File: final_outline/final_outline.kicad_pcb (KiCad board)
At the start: 2 copper layers, 99.5 x 90 mm, 32 parts, among them P001 CANCONNECTOR, P002 AUXCONNECTOR, P100 ISP, P101 DEBUG_LED, U401 ISO1050, U403 LPC11C14, U404 MCP2515_TSSOP, U405 ISO1050, U501 MCP1755

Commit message: board routing in progress
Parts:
- removed C407, C408: 0.1uF, Capacitors_SMD:C_0603_HandSoldering
- removed C409, C410, C411, C412: 1uF, Capacitors_SMD:C_0805_HandSoldering
- removed U404: MCP2515_TSSOP, Housings_SSOP:TSSOP-20_4.4x6.5mm_Pitch0.65mm
- removed U405: ISO1050, Housings_SSOP:MSOP-8_3x3mm_Pitch0.65mm
- moved R201 41.8 mm to (122.6, 108.6)
- moved R401 25.8 mm to (110.5, 47.6), turned to 0 degrees
- moved R402 24.1 mm to (110.5, 50.8), turned to 0 degrees
- moved C406 15.3 mm to (132.1, 78.7), turned to 270 degrees
- moved U501 12.8 mm to (142.2, 101.9)
- moved C404 9.02 mm to (118.1, 94.0)
- moved C405 8.95 mm to (129.5, 78.7), turned to 270 degrees
- moved C401 8.49 mm to (123.8, 94.0)
- moved C402 7.96 mm to (123.2, 96.5)
- moved R303 7.87 mm to (171.4, 57.1), turned to 270 degrees
- moved R305 7.87 mm to (179.1, 57.1), turned to 270 degrees
- moved R306 7.87 mm to (182.9, 57.1)
- moved R302 7.70 mm to (167.6, 57.1), turned to 270 degrees
- moved R307 7.70 mm to (186.7, 57.1), turned to 270 degrees
- moved U401 7.62 mm to (120.7, 101.8)
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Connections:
- net Net-(U401-Pad2) renamed /Micro_Controller/CAN_RXD
- net Net-(U401-Pad3) renamed /Micro_Controller/CAN_TXD
- C401 pad 1: /BACK_PANEL/CANH -> +5V
- C402 pad 1: /BACK_PANEL/CANH -> +5V
- C403 pad 1: /Micro_Controller/+3V3 -> +3V3
- C404 pad 1: /Micro_Controller/+3V3 -> +3V3
- C405 pad 1: /Micro_Controller/+3V3 -> +3V3
- C406 pad 1: /Micro_Controller/+3V3 -> +3V3
- P001 pad 1: Net-(P001-Pad1) -> /BACK_PANEL/CANL
- P001 pad 2: Net-(P001-Pad1) -> /BACK_PANEL/CANH
- P001 pad 3: /BACK_PANEL/CANH -> GND
- P001 pad 4: /BACK_PANEL/CANH -> +5V
- P001 pad 5: GND -> +5V
- P001 pad 7: Net-(P001-Pad7) -> /BACK_PANEL/CANL
- P001 pad 8: Net-(P001-Pad7) -> /BACK_PANEL/CANH
- P100 pad 1: /FRONT_PANEL/+5V -> /FRONT_PANEL/MCU_RESET_N
- P100 pad 2: /FRONT_PANEL/RXD -> GND
- P100 pad 3: /FRONT_PANEL/TXD -> /FRONT_PANEL/RXD
- P100 pad 4: /FRONT_PANEL/MCU_RESET_N -> /FRONT_PANEL/MCU_PROG_N
- P100 pad 5: /FRONT_PANEL/MCU_PROG_N -> +5V
- P100 pad 6: GND -> /FRONT_PANEL/TXD
- P101 pad 11: GND -> Net-(P101-Pad11)
- P101 pad 13: GND -> Net-(P101-Pad13)
- P101 pad 15: GND -> Net-(P101-Pad15)
- P101 pad 2: Net-(P101-Pad2) -> GND
- P101 pad 4: Net-(P101-Pad4) -> GND
- P101 pad 6: Net-(P101-Pad6) -> GND
- P101 pad 8: Net-(P101-Pad8) -> GND
- P101 pad 9: GND -> Net-(P101-Pad9)
- R201 pad 1: /BACK_PANEL/CANH -> /BACK_PANEL/CANL
- R201 pad 2: GND -> /BACK_PANEL/CANH
- R301 pad 2: Net-(P101-Pad2) -> Net-(P101-Pad9)
- R302 pad 1: /FRONT_PANEL/LED2 -> Net-(P101-Pad10)
- R302 pad 2: Net-(P101-Pad6) -> /FRONT_PANEL/LED1
- R303 pad 1: /FRONT_PANEL/LED4 -> Net-(P101-Pad11)
- R303 pad 2: Net-(P101-Pad10) -> /FRONT_PANEL/LED2
- R304 pad 1: /FRONT_PANEL/LED6 -> /FRONT_PANEL/LED3
- R304 pad 2: Net-(P101-Pad14) -> Net-(P101-Pad12)
- R305 pad 1: /FRONT_PANEL/LED1 -> Net-(P101-Pad13)
- R305 pad 2: Net-(P101-Pad4) -> /FRONT_PANEL/LED4
- R306 pad 1: /FRONT_PANEL/LED3 -> /FRONT_PANEL/LED5
- R306 pad 2: Net-(P101-Pad8) -> Net-(P101-Pad14)
- R307 pad 1: /FRONT_PANEL/LED5 -> Net-(P101-Pad15)
- R307 pad 2: Net-(P101-Pad12) -> /FRONT_PANEL/LED6
- R401 pad 1: /Micro_Controller/+3V3 -> +3V3
- R402 pad 1: /Micro_Controller/+3V3 -> +3V3
- U401 pad 1: /Micro_Controller/+3V3 -> +3V3
- U401 pad 6: GND -> /BACK_PANEL/CANL
- U401 pad 8: /BACK_PANEL/CANH -> +5V
- U403 pad 1: /FRONT_PANEL/LED1 -> /FRONT_PANEL/LED3
- U403 pad 11: /FRONT_PANEL/LED2 -> /FRONT_PANEL/LED1
- U403 pad 12: /FRONT_PANEL/LED3 -> /FRONT_PANEL/LED0
- U403 pad 36: /FRONT_PANEL/LED4 -> /FRONT_PANEL/LED7
- U403 pad 37: /FRONT_PANEL/LED5 -> /FRONT_PANEL/LED6
- U403 pad 43: /FRONT_PANEL/LED6 -> /FRONT_PANEL/LED5
- U403 pad 44: /Micro_Controller/+3V3 -> +3V3
- U403 pad 48: /FRONT_PANEL/LED7 -> /FRONT_PANEL/LED4
- U403 pad 8: /Micro_Controller/+3V3 -> +3V3
- U403 pad 9: /FRONT_PANEL/LED0 -> /FRONT_PANEL/LED2
- U501 pad 1: /FRONT_PANEL/+5V -> +5V
- U501 pad 3: /FRONT_PANEL/+5V -> +5V
- U501 pad 5: /Micro_Controller/+3V3 -> +3V3
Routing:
- net /FRONT_PANEL/LED2: track 0.00 -> 58.8 mm
- net /FRONT_PANEL/LED1: track 0.00 -> 56.1 mm
- net /FRONT_PANEL/LED0: track 0.00 -> 53.7 mm
- net /FRONT_PANEL/RXD: track 0.00 -> 31.6 mm, vias 0 -> 1
- net /FRONT_PANEL/MCU_RESET_N: track 0.00 -> 29.3 mm, vias 0 -> 1
- net /Micro_Controller/CAN_RXD: track 0.00 -> 29.3 mm, vias 0 -> 2
- net /Micro_Controller/CAN_TXD: track 0.00 -> 27.9 mm
- net /FRONT_PANEL/TXD: track 0.00 -> 27.6 mm, vias 0 -> 1
- net /BACK_PANEL/CANH: track 0.00 -> 26.2 mm
- net /BACK_PANEL/CANL: track 0.00 -> 26.0 mm
- net /FRONT_PANEL/MCU_PROG_N: track 0.00 -> 25.4 mm, vias 0 -> 1
- net +3V3: track 0.00 -> 13.5 mm
- net +5V: track 0.00 -> 11.8 mm
- net GND: track 0.00 -> 10.4 mm
- added copper zone on F.Cu, net GND
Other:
- net class Default: via_dia 0.6 -> 0.8
- net class POWER added: clearance 0.2, trace_width 0.5, via_dia 0.8, via_drill 0.4

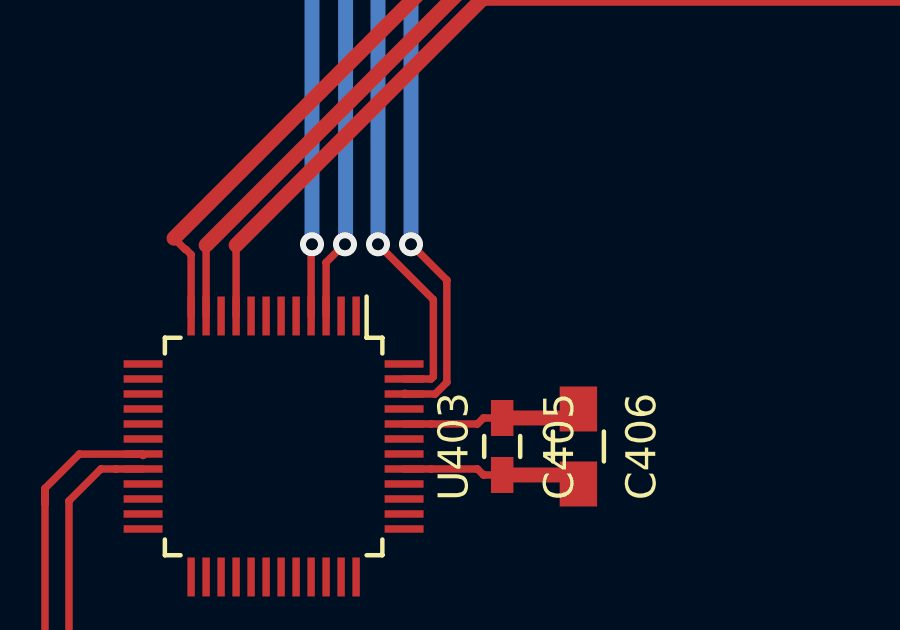
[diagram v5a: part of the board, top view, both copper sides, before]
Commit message: board layout in progress, TODO: power plane, ground plane, finish routing LEDs, connectors
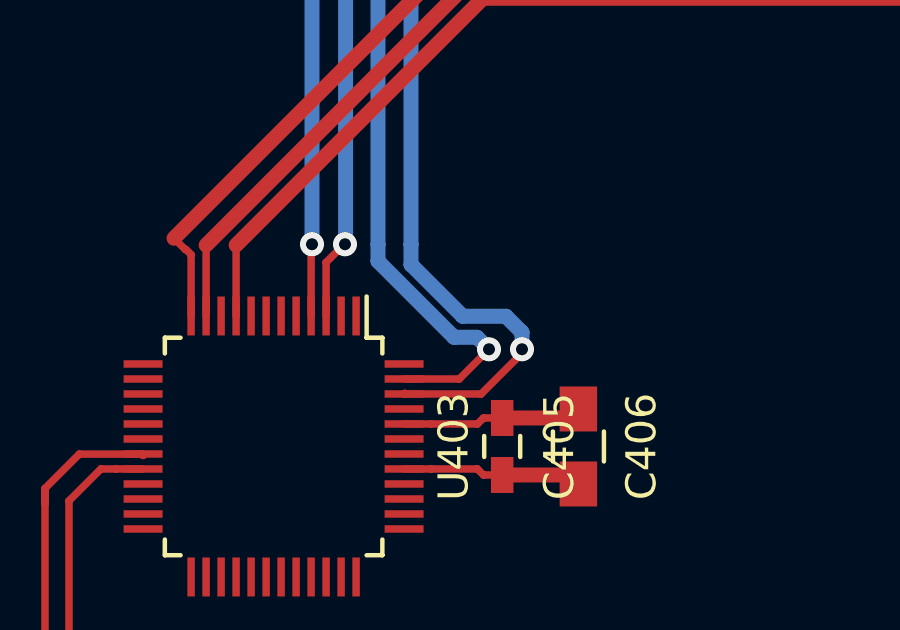
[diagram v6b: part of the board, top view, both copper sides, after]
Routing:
- net /FRONT_PANEL/RXD: track 31.6 -> 35.4 mm
- net /FRONT_PANEL/TXD: track 27.6 -> 30.2 mm
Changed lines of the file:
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@@
   (general
     (links 67)
-    (no_connects 47)
+    (no_connects 44)
     (area 102.424999 35.115 215 136.499792)
     (thickness 1.6)
     (drawings 6)
-    (tracks 124)
+    (tracks 130)
     (zones 0)
     (modules 24)
@@
   (segment (start 123.17 72.03) (end 123.2 72) (width 0.25) (layer F.Cu) (net 32))
   (via (at 123.2 72) (size 0.8) (drill 0.4) (layers F.Cu B.Cu) (net 32))
+  (segment (start 128.224277 74.4) (end 126.5 72.675723) (width 0.5) (layer B.Cu) (net 33))
+  (segment (start 126.5 72.675723) (end 126.5 72) (width 0.5) (layer B.Cu) (net 33))
+  (segment (start 130.2 75.5) (end 130.2 74.934315) (width 0.5) (layer B.Cu) (net 33))
+  (segment (start 130.2 74.934315) (end 129.665685 74.4) (width 0.5) (layer B.Cu) (net 33))
+  (segment (start 129.665685 74.4) (end 128.224277 74.4) (width 0.5) (layer B.Cu) (net 33))
+  (segment (start 126.27 76.99) (end 128.839999 76.99) (width 0.25) (layer F.Cu) (net 33))
+  (segment (start 128.839999 76.99) (end 130.2 75.629999) (width 0.25) (layer F.Cu) (net 33))
+  (segment (start 130.2 75.629999) (end 130.2 75.5) (width 0.25) (layer F.Cu) (net 33))
+  (via (at 130.2 75.5) (size 0.8) (drill 0.4) (layers F.Cu B.Cu) (net 33))
   (segment (start 126.5 72) (end 126.5 49.33) (width 0.5) (layer B.Cu) (net 33))
   (segment (start 126.5 49.33) (end 124.92 47.75) (width 0.5) (layer B.Cu) (net 33))
-  (segment (start 126.27 76.99) (end 127.30641 76.99) (width 0.25) (layer F.Cu) (net 33))
-  (segment (start 127.30641 76.99) (end 127.695011 76.601399) (width 0.25) (layer F.Cu) (net 33))
-  (via (at 126.5 72) (size 0.8) (drill 0.4) (layers F.Cu B.Cu) (net 33))
-  (segment (start 127.695011 76.601399) (end 127.695011 73.195011) (width 0.25) (layer F.Cu) (net 33))
-  (segment (start 127.695011 73.195011) (end 126.5 72) (width 0.25) (layer F.Cu) (net 33))
   (segment (start 126.27 76.99) (end 126.298 76.962) (width 0.25) (layer F.Cu) (net 33))
+  (segment (start 129.1 75.5) (end 128.700001 75.100001) (width 0.5) (layer B.Cu) (net 34))
+  (segment (start 128.700001 75.100001) (end 127.934316 75.100001) (width 0.5) (layer B.Cu) (net 34))
+  (segment (start 127.934316 75.100001) (end 125.4 72.565685) (width 0.5) (layer B.Cu) (net 34))
+  (segment (start 125.4 72.565685) (end 125.4 72) (width 0.5) (layer B.Cu) (net 34))
+  (segment (start 126.27 76.49) (end 128.11 76.49) (width 0.25) (layer F.Cu) (net 34))
+  (segment (start 128.11 76.49) (end 129.1 75.5) (width 0.25) (layer F.Cu) (net 34))
+  (via (at 129.1 75.5) (size 0.8) (drill 0.4) (layers F.Cu B.Cu) (net 34))
   (segment (start 125.4 72) (end 125.4 51.23) (width 0.5) (layer B.Cu) (net 34))
   (segment (start 125.4 51.23) (end 124.92 50.75) (width 0.5) (layer B.Cu) (net 34))
-  (segment (start 126.27 76.49) (end 127.17 76.49) (width 0.25) (layer F.Cu) (net 34))
-  (segment (start 127.17 76.49) (end 127.245001 76.414999) (width 0.25) (layer F.Cu) (net 34))
-  (segment (start 127.245001 76.414999) (end 127.245001 73.845001) (width 0.25) (layer F.Cu) (net 34))
-  (segment (start 127.245001 73.845001) (end 125.4 72) (width 0.25) (layer F.Cu) (net 34))
-  (via (at 125.4 72) (size 0.8) (drill 0.4) (layers F.Cu B.Cu) (net 34))
   (segment (start 157.5 62.39998) (end 161.56998 58.33) (width 0.5) (layer F.Cu) (net 35))
   (segment (start 161.56998 58.33) (end 163.83 58.33) (width 0.5) (layer F.Cu) (net 35))

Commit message: Working on routing the PCB
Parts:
- moved P100 62.7 mm to (179.9, 62.2)
- moved R301 50.5 mm to (115.3, 71.2)
- moved R305 50.5 mm to (130.5, 71.2)
- moved R306 50.5 mm to (134.3, 71.2)
- moved R307 50.5 mm to (138.2, 71.2)
- moved R308 50.5 mm to (142.0, 71.4)
- moved R302 50.5 mm to (119.1, 71.2)
- moved R303 50.5 mm to (122.9, 71.2)
- moved R304 50.5 mm to (126.7, 71.4)
- moved P101 50.5 mm to (118.0, 62.0)
- moved R402 49.7 mm to (149.0, 82.2), turned to 90 degrees
- moved R401 49.4 mm to (145.8, 82.2), turned to 90 degrees
- moved C404 12.2 mm to (130.2, 95.9), turned to 270 degrees
- moved C401 9.92 mm to (130.2, 101.6), turned to 90 degrees
- moved C403 8.89 mm to (127.6, 96.5), turned to 270 degrees
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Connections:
- U403 pad 39: /Micro_Controller/PIO1_3 -> /FRONT_PANEL/LED5
- U403 pad 43: /FRONT_PANEL/LED5 -> /Micro_Controller/PIO3_2
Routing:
- net +3V3: track 13.5 -> 69.4 mm, vias 0 -> 2
- net /FRONT_PANEL/LED2: track 58.8 -> 7.24 mm
- net /FRONT_PANEL/LED1: track 56.1 -> 8.47 mm
- net /FRONT_PANEL/LED0: track 53.7 -> 10.7 mm
- net +5V: track 11.8 -> 48.9 mm, vias 0 -> 1
- net /FRONT_PANEL/LED7: track 0.00 -> 28.3 mm, vias 0 -> 2
- net /FRONT_PANEL/LED6: track 0.00 -> 22.9 mm, vias 0 -> 2
- net /FRONT_PANEL/RXD: track 35.4 -> 16.5 mm, vias 1 -> 0
- net /FRONT_PANEL/LED5: track 0.00 -> 16.7 mm, vias 0 -> 2
- net /FRONT_PANEL/TXD: track 30.2 -> 16.2 mm, vias 1 -> 0
- net /FRONT_PANEL/LED4: track 0.00 -> 11.1 mm
- net /FRONT_PANEL/MCU_PROG_N: track 25.4 -> 33.3 mm, vias 1 -> 2
- net /FRONT_PANEL/LED3: track 0.00 -> 6.91 mm
- net Net-(P101-Pad16): track 0.00 -> 6.53 mm
- net Net-(P101-Pad9): track 0.00 -> 6.25 mm
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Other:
- board size 99.5 x 90 mm -> 99.5 x 75 mm

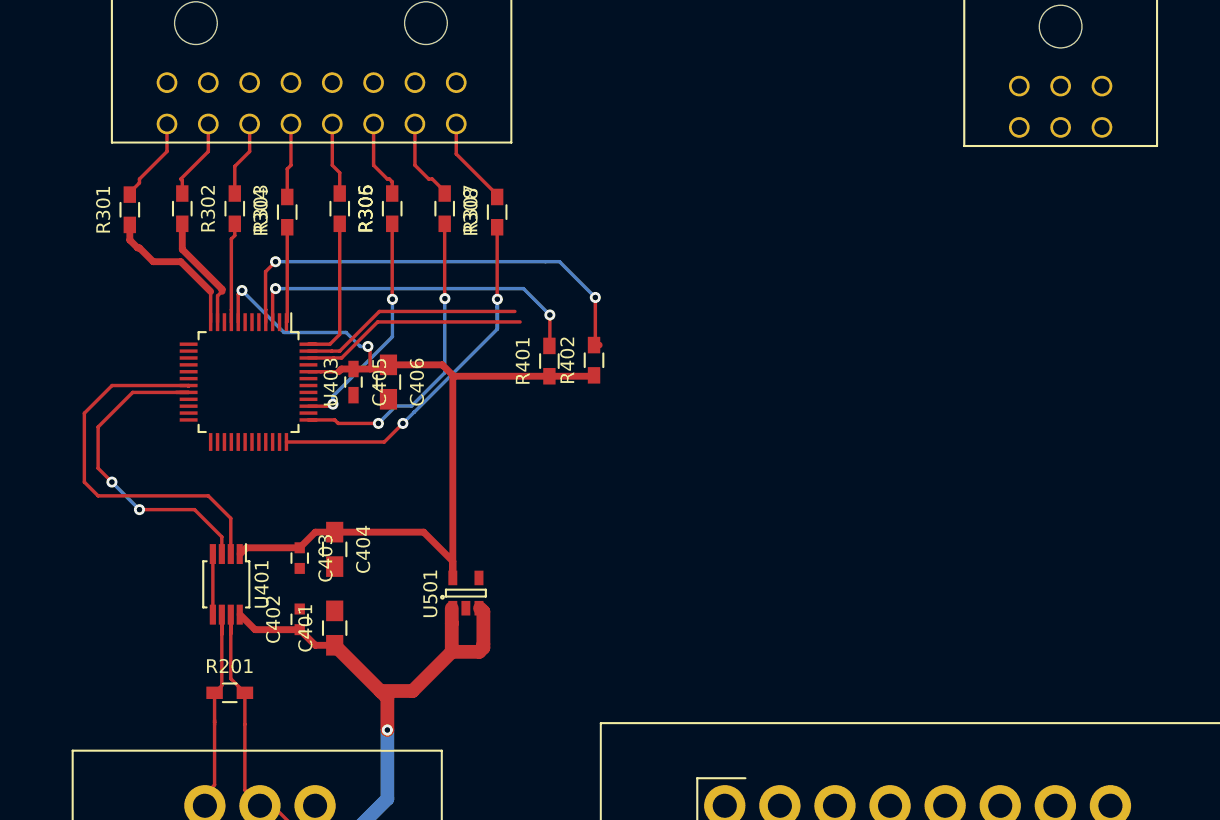
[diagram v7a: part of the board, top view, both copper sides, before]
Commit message: Changed some pin-outs, more routing
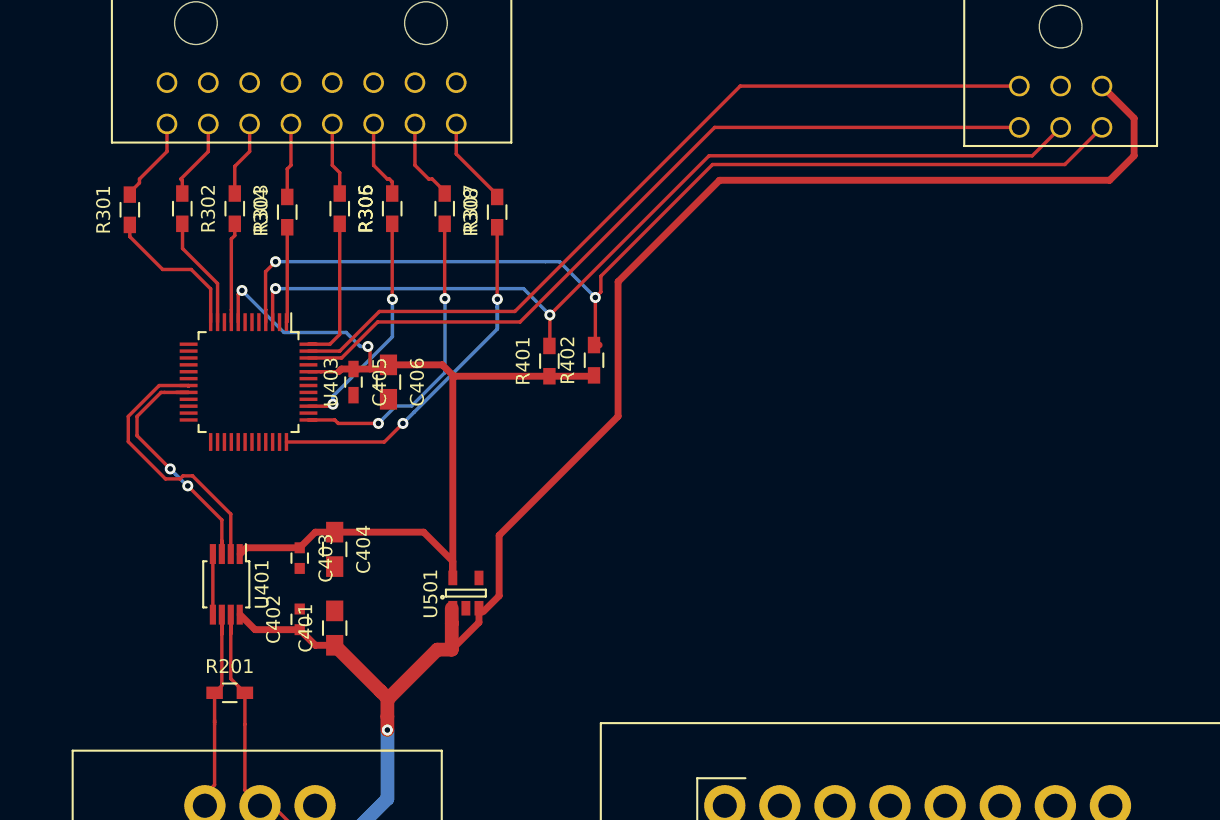
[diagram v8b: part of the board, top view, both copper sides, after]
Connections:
- P100 pad 1: /FRONT_PANEL/MCU_RESET_N -> /FRONT_PANEL/TXD
- P100 pad 3: /FRONT_PANEL/RXD -> +5V
- P100 pad 4: /FRONT_PANEL/MCU_PROG_N -> /FRONT_PANEL/RXD
- P100 pad 5: +5V -> /FRONT_PANEL/MCU_RESET_N
- P100 pad 6: /FRONT_PANEL/TXD -> /FRONT_PANEL/MCU_PROG_N
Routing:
- net +5V: track 48.9 -> 122.1 mm
- net /FRONT_PANEL/TXD: track 16.2 -> 59.6 mm
- net /FRONT_PANEL/MCU_RESET_N: track 25.5 -> 68.3 mm
- net /FRONT_PANEL/MCU_PROG_N: track 33.3 -> 75.9 mm
- net /FRONT_PANEL/RXD: track 16.5 -> 58.5 mm
- net /Micro_Controller/CAN_RXD: track 27.8 -> 20.0 mm
- net /Micro_Controller/CAN_TXD: track 23.9 -> 19.2 mm
